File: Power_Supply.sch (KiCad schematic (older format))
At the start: 68 parts, among them IC2 ADR127BUJZ-REEL7, Q1 FDS9926A, Q3 FDV301N, U5 ADP5052ACPZ-R7

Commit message: Added Sheet FPGA_Banks Drawn the connections of FPGA and RAM Completed the top sheet connections
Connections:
- net at U5.12 (BST4): now also C19.1
- net at U5.3 (SW3): now also C18.2, L3.2
- net at U5.45 (FB3): now also R19.2
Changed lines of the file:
@@
 $Descr A4 11693 8268
 encoding utf-8
-Sheet 12 21
+Sheet 12 22
 Title ""
 Date ""

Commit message: Rearranged the top sheet blocks modified hir. pins in few blocks
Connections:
- net at U5.12 (BST4): now also C19.1
- net at U5.3 (SW3): now also C18.2, L3.2
- net at U5.45 (FB3): now also R19.2
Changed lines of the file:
@@
 $Descr A4 11693 8268
 encoding utf-8
-Sheet 12 22
+Sheet 11 22
 Title ""
 Date ""

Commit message: Added ADC schematic
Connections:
- net at U5.12 (BST4): now also C19.1
- net at U5.3 (SW3): now also C18.2, L3.2
- net at U5.45 (FB3): now also R19.2
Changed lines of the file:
@@
 $Descr A4 11693 8268
 encoding utf-8
-Sheet 11 22
+Sheet 11 25
 Title ""
 Date ""

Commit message: -Clock --GND pin was missing. it was added to pin 45 -BTB --pins added
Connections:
- net at U5.12 (BST4): now also C19.1
- net at U5.3 (SW3): now also C18.2, L3.2
- net at U5.45 (FB3): now also R19.2
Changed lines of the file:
@@
 $Descr A4 11693 8268
 encoding utf-8
-Sheet 11 25
+Sheet 9 25
 Title ""
 Date ""

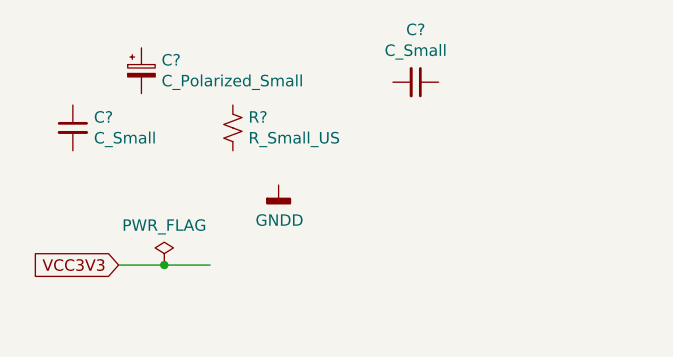
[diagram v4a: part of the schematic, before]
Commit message: PCB created and schematics annotated High speed connections added to the BTB
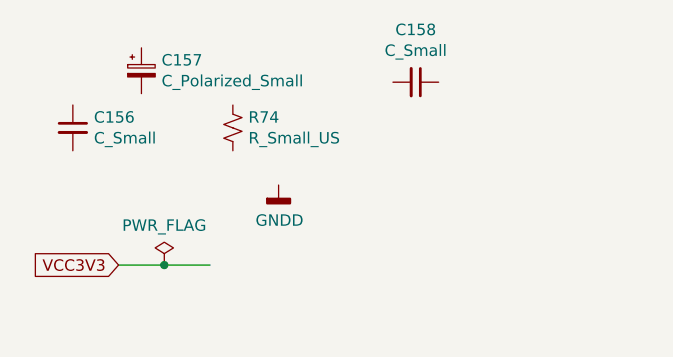
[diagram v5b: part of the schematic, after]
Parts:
- gave numbers to parts that had none: 4
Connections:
- net at U5.12 (BST4): now also C19.1
- net at U5.3 (SW3): now also C18.2, L3.2
- net at U5.45 (FB3): now also R19.2
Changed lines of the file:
@@
 Connection ~ 1900 1000
 $Comp
-L power:PWR_FLAG #FLG?
+L power:PWR_FLAG #FLG030
 U 1 1 602F5542
 P 1900 1000
-F 0 "#FLG?" H 1900 1075 50  0001 C CNN
+F 0 "#FLG030" H 1900 1075 50  0001 C CNN
 F 1 "PWR_FLAG" H 1900 1173 50  0000 C CNN
 F 2 "" H 1900 1000 50  0001 C CNN
@@
 AR Path="/601E7C92/60257FE5/603121C7" Ref="R?"  Part="1"
 AR Path="/601E7B38/603121C7" Ref="R?"  Part="1"
-AR Path="/601DF0A6/603121C7" Ref="R?"  Part="1"
-F 0 "R?" H -1282 846 50  0000 L CNN
+AR Path="/601DF0A6/603121C7" Ref="R74"  Part="1"
+F 0 "R74" H -1282 846 50  0000 L CNN
 F 1 "R_Small_US" H -1282 755 50  0000 L CNN
 F 2 "Resistor_SMD:R_0603_1608Metric_Pad0.98x0.95mm_HandSolder" H -1350 800 50  0001 C CNN
@@
 AR Path="/601E7C92/60257FE5/603121CE" Ref="C?"  Part="1"
 AR Path="/601E7B38/603121CE" Ref="C?"  Part="1"
-AR Path="/601DF0A6/603121CE" Ref="C?"  Part="1"
-F 0 "C?" H -1958 846 50  0000 L CNN
+AR Path="/601DF0A6/603121CE" Ref="C156"  Part="1"
+F 0 "C156" H -1958 846 50  0000 L CNN
 F 1 "C_Small" H -1958 755 50  0000 L CNN
 F 2 "Capacitor_SMD:C_0603_1608Metric_Pad1.08x0.95mm_HandSolder" H -2050 800 50  0001 C CNN
@@
 AR Path="/601E7C92/60257FE5/603121D5" Ref="#FLG?"  Part="1"
 AR Path="/601E7B38/603121D5" Ref="#FLG?"  Part="1"
-AR Path="/601DF0A6/603121D5" Ref="#FLG?"  Part="1"
-F 0 "#FLG?" H -1650 1475 50  0001 C CNN
+AR Path="/601DF0A6/603121D5" Ref="#FLG029"  Part="1"
+F 0 "#FLG029" H -1650 1475 50  0001 C CNN
 F 1 "PWR_FLAG" H -1650 1573 50  0000 C CNN
 F 2 "" H -1650 1400 50  0001 C CNN
@@
 	-1850 1400 -1650 1400
 $Comp
-L power:GNDD #PWR?
+L power:GNDD #PWR078
 U 1 1 603121DE
 P -1150 1050
-AR Path="/601DF0A6/603121DE" Ref="#PWR?"  Part="1"
+AR Path="/601DF0A6/603121DE" Ref="#PWR078"  Part="1"
 AR Path="/601E7C5A/603121DE" Ref="#PWR?"  Part="1"
 AR Path="/601E7CC8/603121DE" Ref="#PWR?"  Part="1"
@@
 AR Path="/601E7C92/60257FE5/603121DE" Ref="#PWR?"  Part="1"
 AR Path="/601E7B38/603121DE" Ref="#PWR?"  Part="1"
-F 0 "#PWR?" H -1150 800 50  0001 C CNN
+F 0 "#PWR078" H -1150 800 50  0001 C CNN
 F 1 "GNDD" H -1146 895 50  0000 C CNN
 F 2 "" H -1150 1050 50  0001 C CNN
@@
 AR Path="/601E7C92/60257FE5/603121E5" Ref="C?"  Part="1"
 AR Path="/601E7B38/603121E5" Ref="C?"  Part="1"
-AR Path="/601DF0A6/603121E5" Ref="C?"  Part="1"
-F 0 "C?" H -1662 596 50  0000 L CNN
+AR Path="/601DF0A6/603121E5" Ref="C157"  Part="1"
+F 0 "C157" H -1662 596 50  0000 L CNN
 F 1 "C_Polarized_Small" H -1662 505 50  0000 L CNN
 F 2 "Capacitor_Tantalum_SMD:CP_EIA-1608-10_AVX-L_Pad1.25x1.05mm_HandSolder" H -1750 550 50  0001 C CNN
@@
 P -550 600
 AR Path="/601E7B38/603121EB" Ref="C?"  Part="1"
-AR Path="/601DF0A6/603121EB" Ref="C?"  Part="1"
-F 0 "C?" V -779 600 50  0000 C CNN
+AR Path="/601DF0A6/603121EB" Ref="C158"  Part="1"
+F 0 "C158" V -779 600 50  0000 C CNN
 F 1 "C_Small" V -688 600 50  0000 C CNN
 F 2 "" H -550 600 50  0001 C CNN

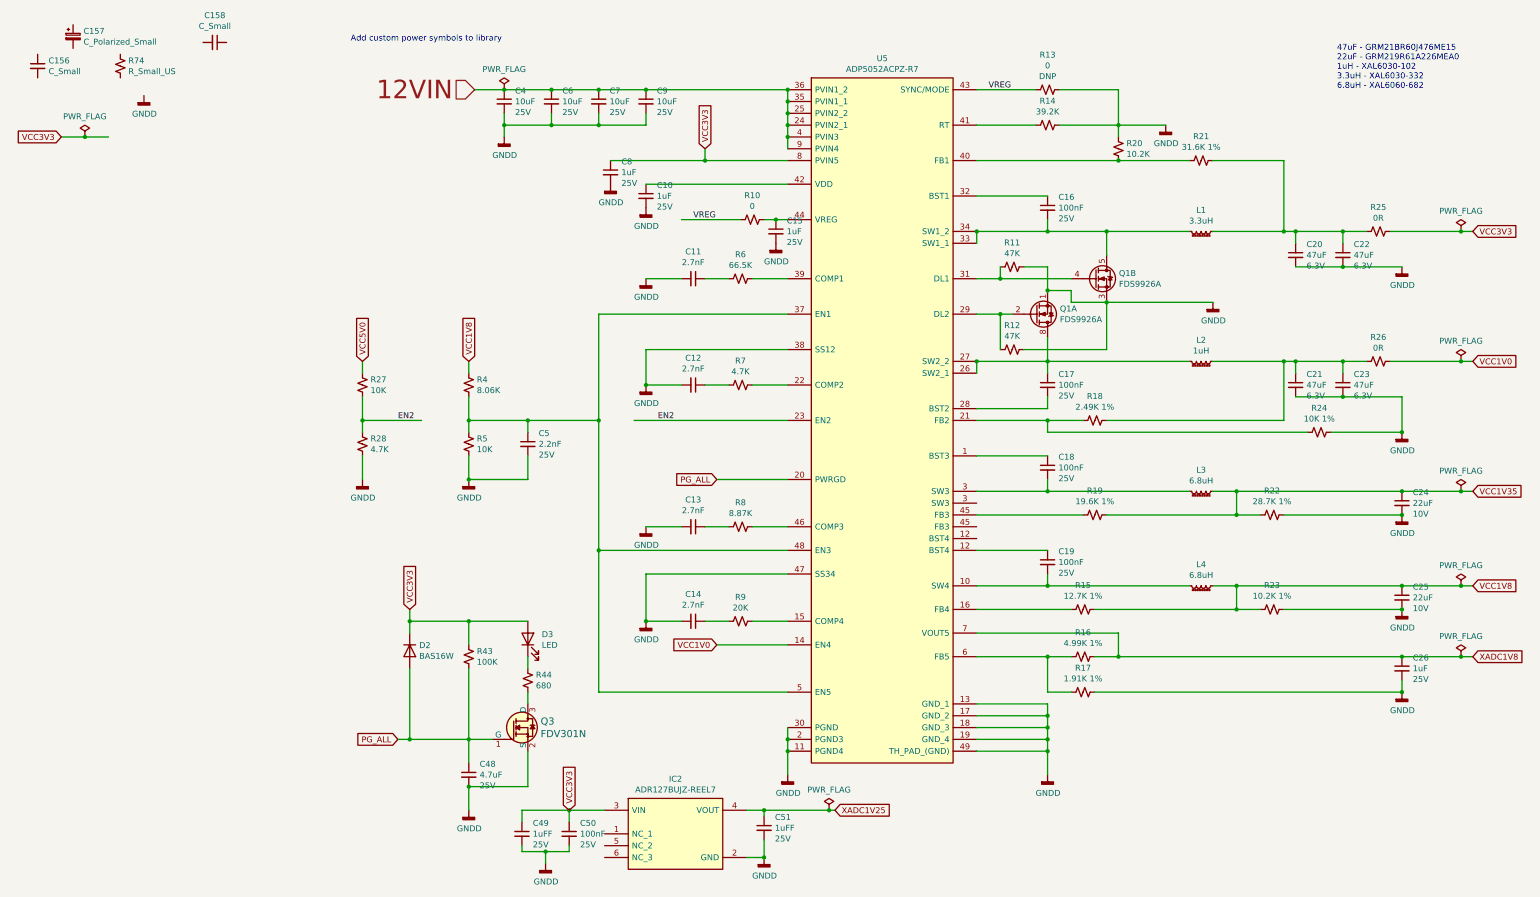
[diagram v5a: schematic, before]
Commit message: Corrected PCB import errors
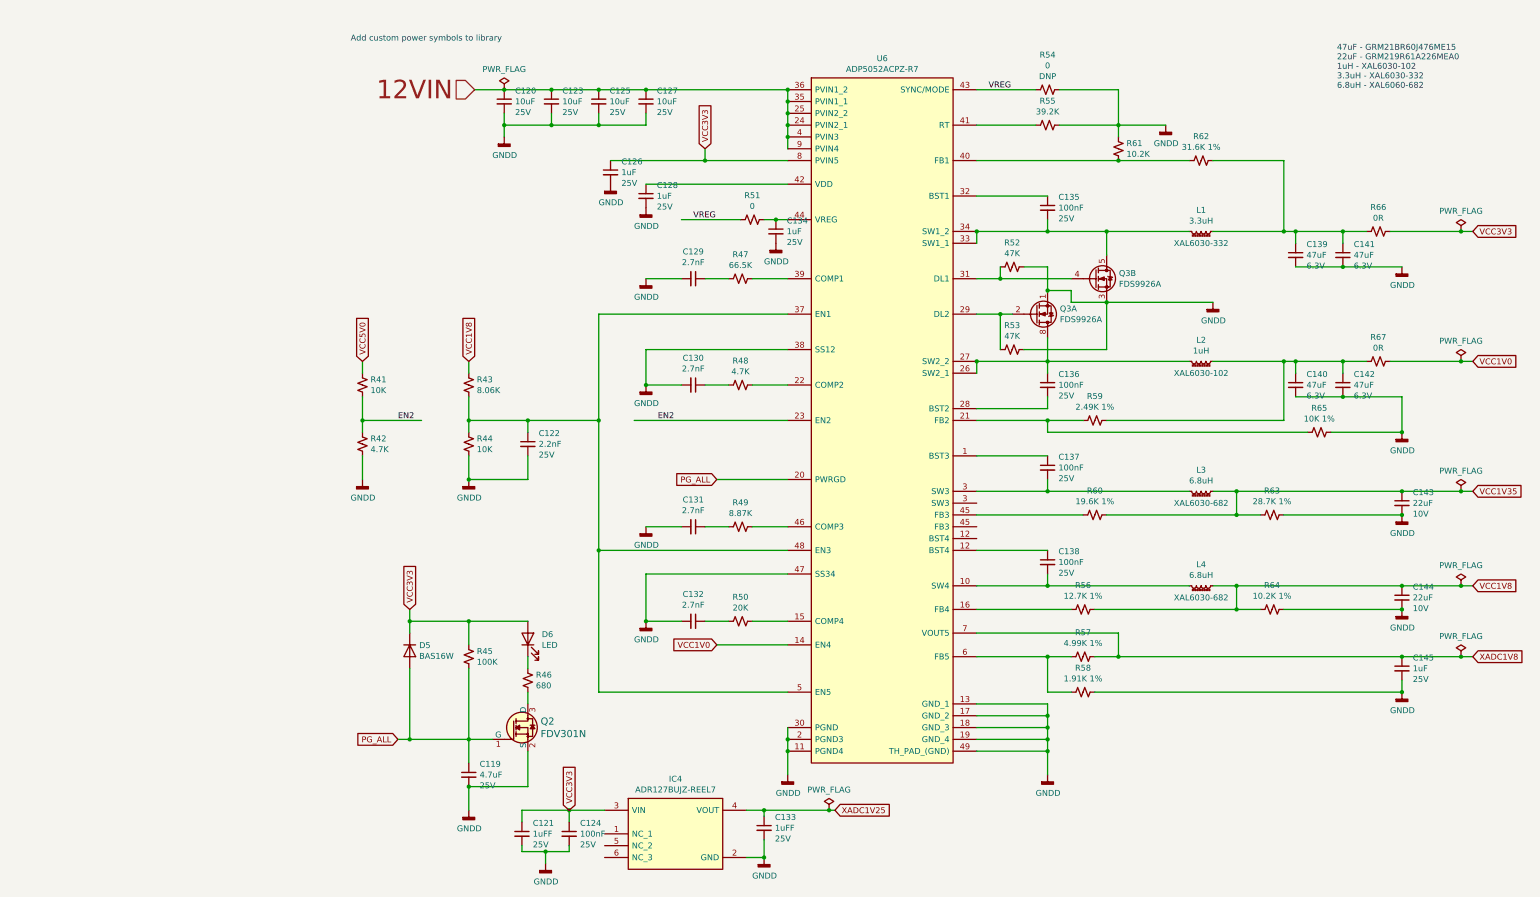
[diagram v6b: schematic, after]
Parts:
- removed C156: C_Small, Capacitor_SMD:C_0603_1608Metric_Pad1.08x0.95mm_HandSolder, symbol Device:C_Small
- removed C157: C_Polarized_Small, Capacitor_Tantalum_SMD:CP_EIA-1608-10_AVX-L_Pad1.25x1.05mm_HandSolder, symbol Device:C_Polarized_Small
- removed C158: C_Small, symbol Device:C_Small
- removed R74: R_Small_US, Resistor_SMD:R_0603_1608Metric_Pad0.98x0.95mm_HandSolder, symbol Device:R_Small_US
- L1: footprint (none) -> Inductor_SMD:L_Coilcraft_XAL60xx_6.36x6.56mm; MPN (none) -> XAL6030-332
- L2: footprint (none) -> Inductor_SMD:L_Coilcraft_XAL60xx_6.36x6.56mm; MPN (none) -> XAL6030-102
- L3, L4: footprint (none) -> Inductor_SMD:L_Coilcraft_XAL60xx_6.36x6.56mm; MPN (none) -> XAL6030-682
- renumbered C48 to C119, C4 to C120, C49 to C121, C5 to C122, C6 to C123, C50 to C124, C7 to C125, C8 to C126, C9 to C127, C10 to C128, C11 to C129, C12 to C130, C13 to C131, C14 to C132, C51 to C133, C15 to C134, C16 to C135, C17 to C136, C18 to C137, C19 to C138, C20 to C139, C21 to C140, C22 to C141, C23 to C142, C24 to C143, C25 to C144, C26 to C145, D2 to D5, D3 to D6, IC2 to IC4, Q3 to Q2, Q1 to Q3, R27 to R41, R28 to R42, R4 to R43, R5 to R44, R43 to R45, R44 to R46, R6 to R47, R7 to R48, R8 to R49, R9 to R50, R10 to R51, R11 to R52, R12 to R53, R13 to R54, R14 to R55, R15 to R56, R16 to R57, R17 to R58, R18 to R59, R19 to R60, R20 to R61, R21 to R62, R22 to R63, R23 to R64, R24 to R65, R25 to R66, R26 to R67, U5 to U6
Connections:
- net at U6.12 (BST4): now also C138.1
- net at U6.3 (SW3): now also C137.2, L3.2
- net at U6.45 (FB3): now also R60.2
